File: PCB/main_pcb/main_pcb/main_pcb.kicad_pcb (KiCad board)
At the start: 2 copper layers, 163.5 x 142.5 mm, 49 parts, among them J1 Conn_01x20_Socket, J2 Conn_01x20_Socket, SW0_Header1 B6B-XH-A, SW1_Header1 B6B-XH-A

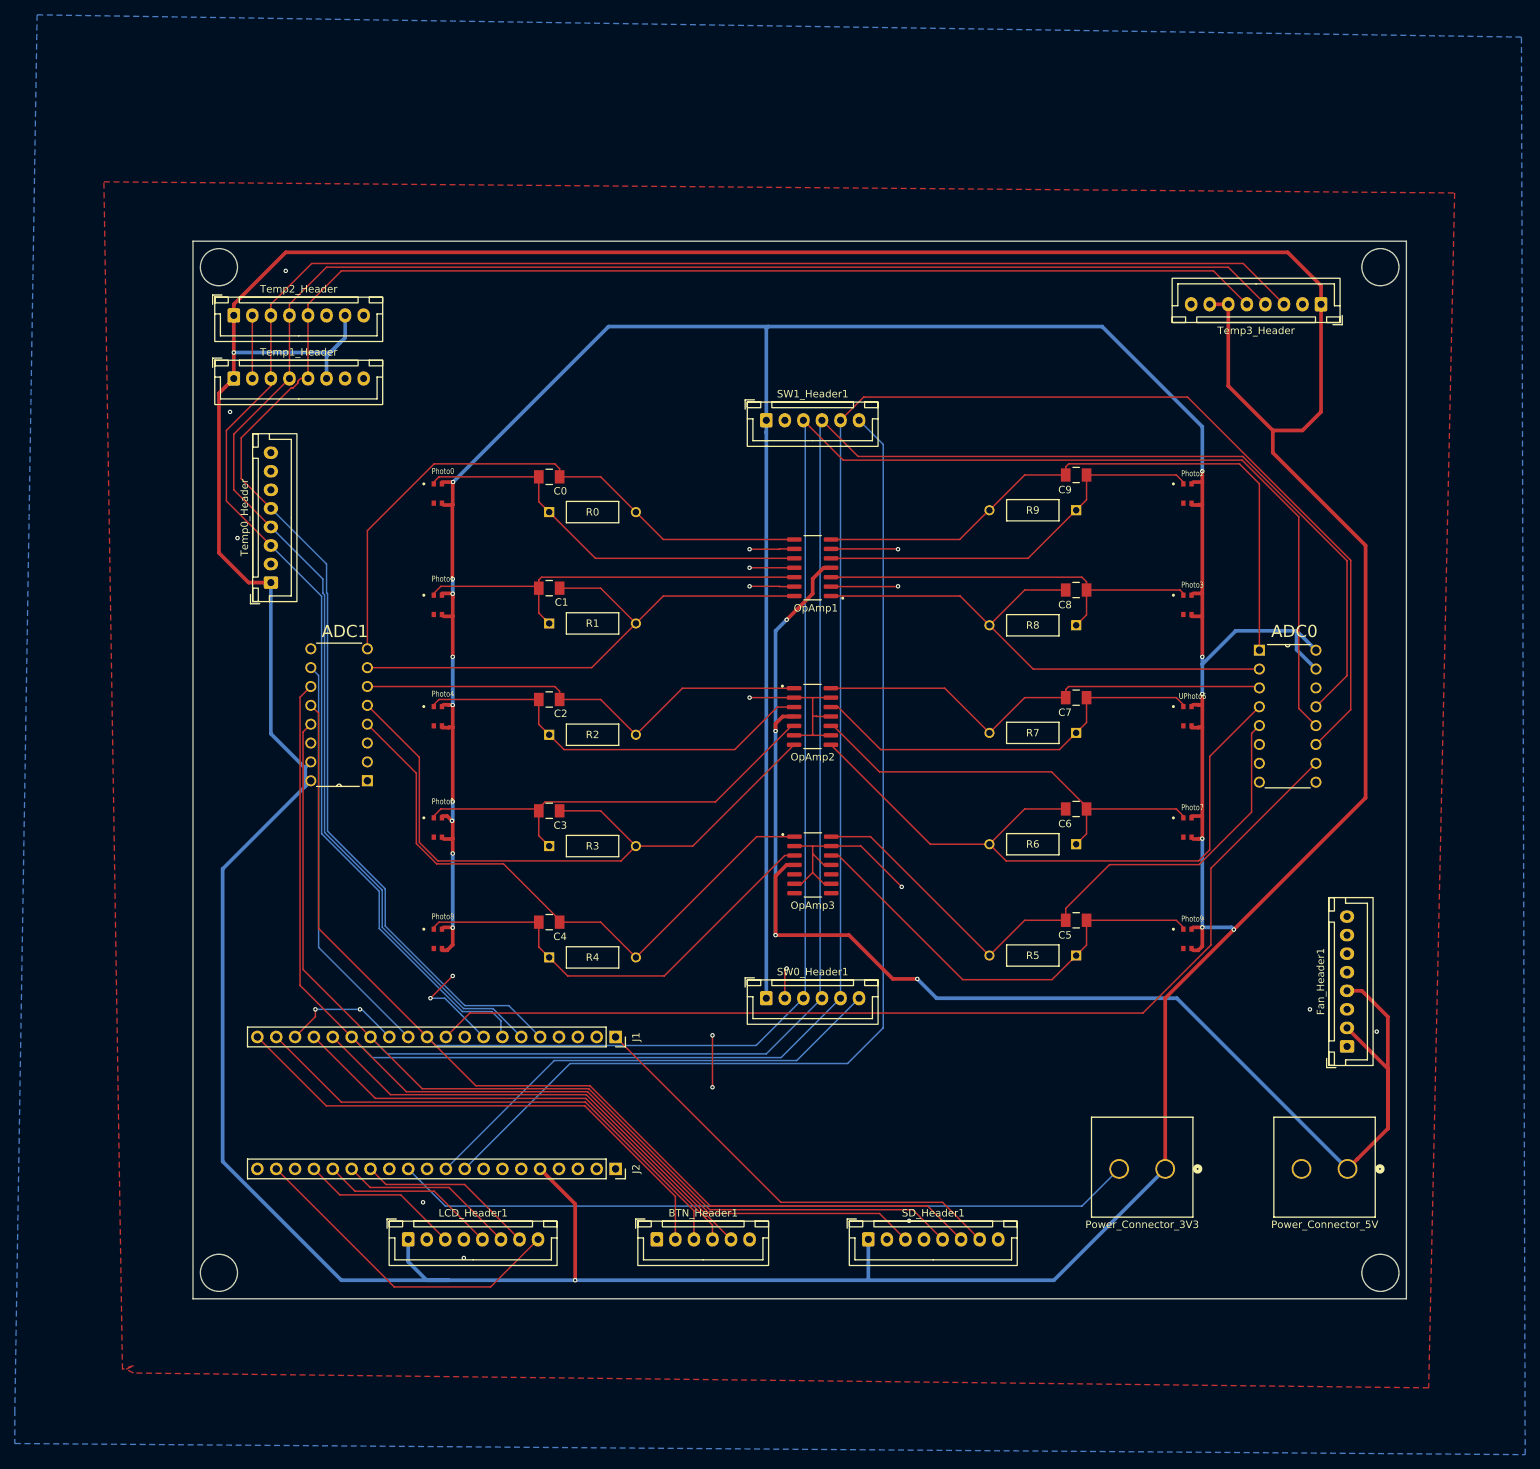
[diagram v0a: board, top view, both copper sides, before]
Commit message: Added heater actuation header.
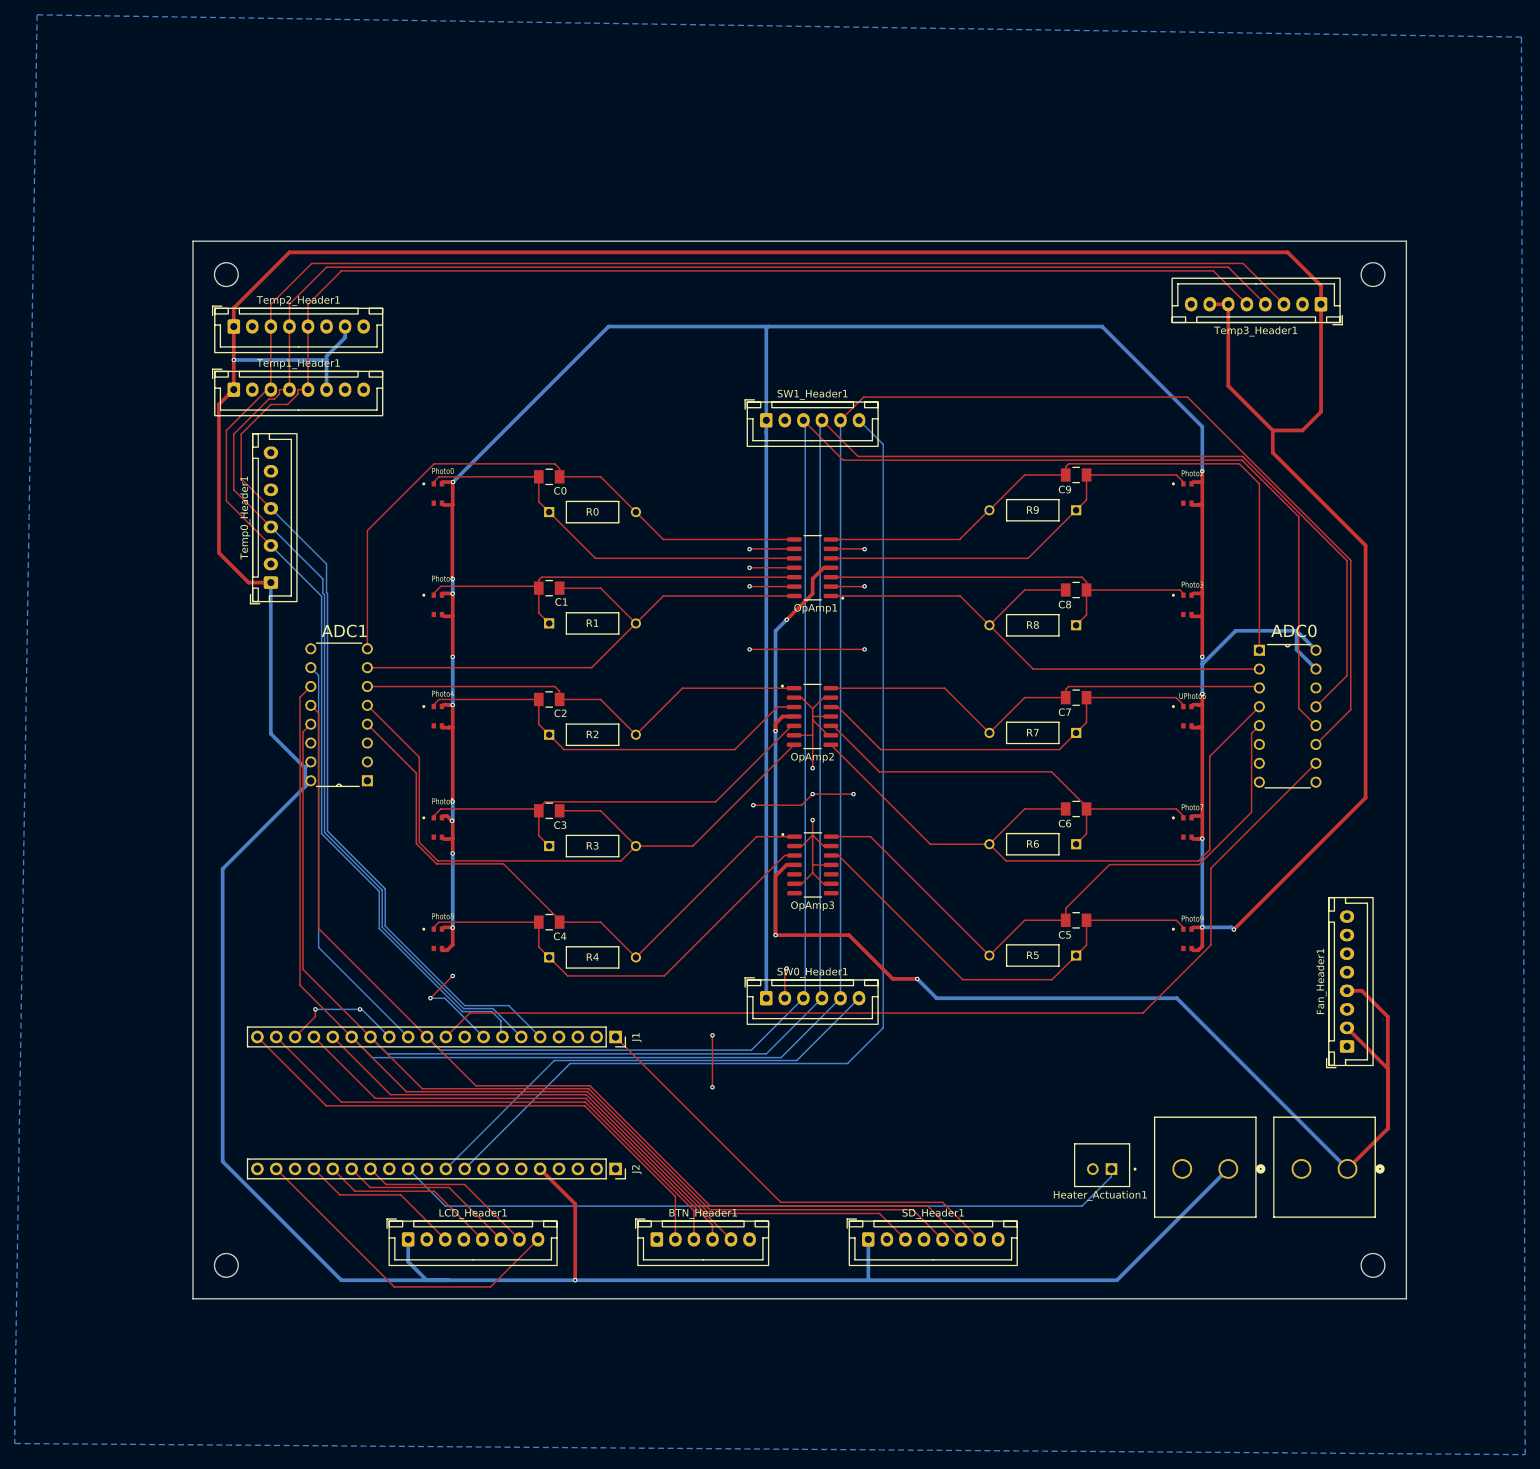
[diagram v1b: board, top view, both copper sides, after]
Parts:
- added Heater_Actuation1: B2B-XH-A, B2B_XH_A:JST_B2B-XH-A, F.Cu at (140.0, 153.0)
- added REF**: MountingHole_3.2mm_M3, MountingHole:MountingHole_3.2mm_M3, F.Cu at (176.5, 33.0)
- added REF**: MountingHole_3.2mm_M3, MountingHole:MountingHole_3.2mm_M3, F.Cu at (22.0, 33.0)
- added REF**: MountingHole_3.2mm_M3, MountingHole:MountingHole_3.2mm_M3, F.Cu at (22.0, 166.5)
- added REF**: MountingHole_3.2mm_M3, MountingHole:MountingHole_3.2mm_M3, F.Cu at (176.5, 166.5)
- moved Power_Connector_3V3 8.50 mm to (157.0, 153.5)
- moved Temp1_Header1 1.50 mm to (23.0, 48.5)
- moved Temp2_Header1 1.50 mm to (23.0, 40.0)
- renumbered Power_Connector_5V to Power_Connector_5V1, Temp0_Header to Temp0_Header1, Temp1_Header to Temp1_Header1, Temp2_Header to Temp2_Header1, Temp3_Header to Temp3_Header1
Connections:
- net SPI0_RX renamed SPI0_MISO
- net SPI0_TX renamed SPI0_MOSI
- net SPI1_RX renamed SPI1_MISO
- net SPI1_TX renamed SPI1_MOSI
- Power_Connector_3V3 pad 2: HEATER_ON -> GND
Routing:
- net +3.3V: track 1034.8 -> 1004.3 mm
- net GND: track 139.1 -> 142.5 mm, vias 22 -> 19
- net TEMP_ALERT: track 253.6 -> 254.9 mm
- net I2C0_SDA: track 255.8 -> 257.1 mm
- net SPI1_MISO: track 367.6 -> 368.1 mm
- removed copper zone on F.Cu, net GND
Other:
- outline, holes or cut-outs redrawn

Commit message: Updated and tweaked main PCB
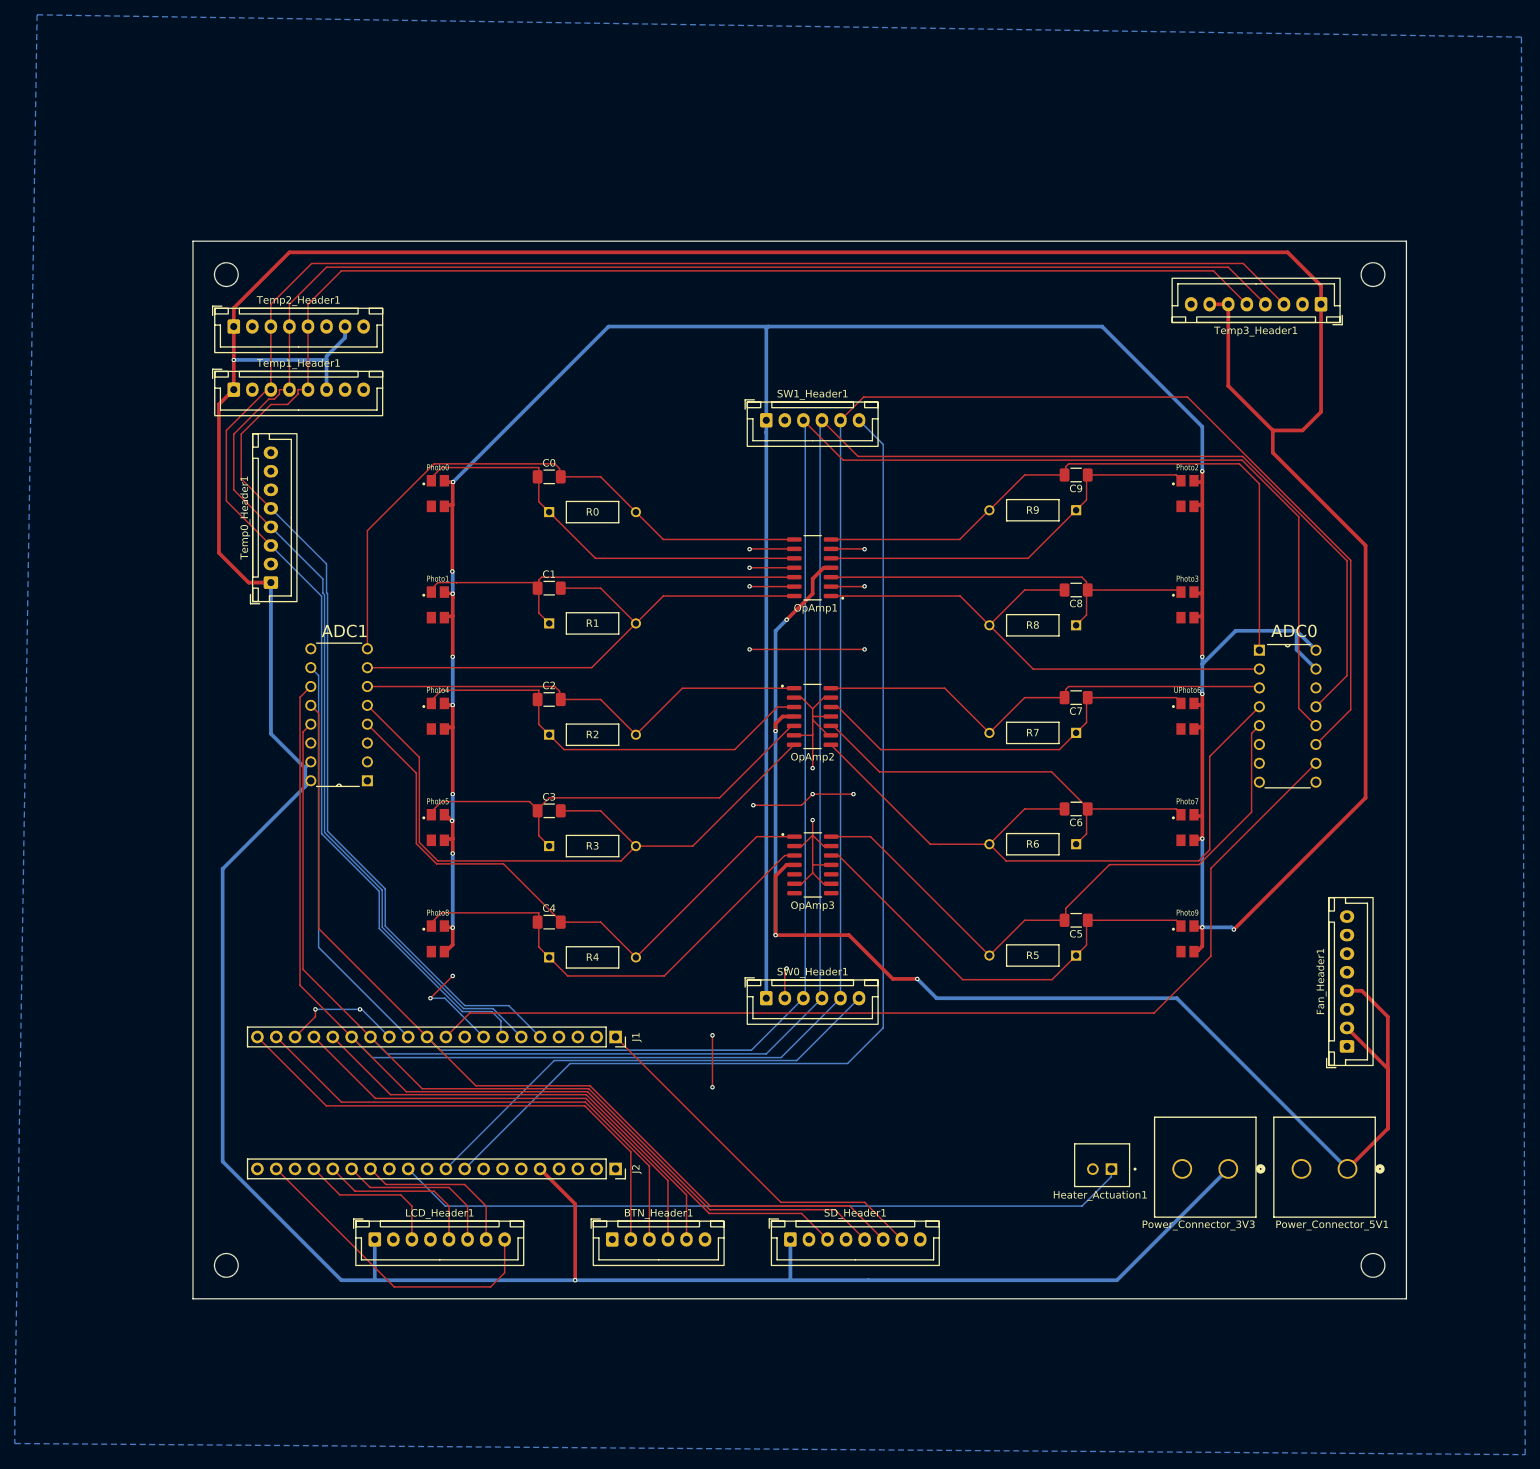
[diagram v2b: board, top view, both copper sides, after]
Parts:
- C0, C1, C2, C3, C4, C5, C6, C7, C8, C9: footprint C1206C101K1HACTU:CAPC340180_88N_KEM -> Capacitor_SMD:C_1206_3216Metric_Pad1.33x1.80mm_HandSolder
- Photo0, Photo1, Photo2, Photo3, Photo4, Photo5, Photo7, Photo8, Photo9, UPhoto6: footprint APDS_9006_020:photodiode_v3 -> APDS_9006_020:photodiode_v4
- moved SD_Header1 10.5 mm to (98.0, 163.0)
- moved BTN_Header1 6.00 mm to (74.0, 163.0)
- moved LCD_Header1 4.50 mm to (42.0, 163.0)
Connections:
- J2 pad 14: DISP REGSEL -> DISP_RST
- J2 pad 15: DISP_RST -> DISP REGSEL
- LCD_Header1 pad 6: DISP_RST -> DISP REGSEL
- LCD_Header1 pad 7: DISP REGSEL -> DISP_RST
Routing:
- net SPI1_SCK: track 377.7 -> 367.2 mm
- net SPI1_MOSI: track 390.7 -> 380.2 mm
- net SPI1_MISO: track 368.1 -> 357.6 mm
- net SPI1_CSn_SD: track 60.4 -> 49.9 mm
- net +3.3V: track 1004.3 -> 1000.3 mm
- net OpIn8: track 60.6 -> 63.3 mm
- net OpIn4: track 56.0 -> 58.5 mm
- net OpIn0: track 55.4 -> 57.9 mm
- net BTN1: track 69.8 -> 67.4 mm
- net BTN3: track 65.0 -> 62.5 mm
- net BTN2: track 66.1 -> 63.6 mm
- net BTN0: track 71.0 -> 68.5 mm
- net DISP_RST: track 24.1 -> 22.2 mm
- net SPI0_SCK: track 21.6 -> 19.8 mm
- net SPI0_MOSI: track 24.1 -> 22.2 mm
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
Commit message: Fixed some stuff and made the main PCB smaller.
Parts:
- added J3: Conn_01x09_Socket, Connector_PinSocket_2.54mm:PinSocket_1x09_P2.54mm_Vertical, F.Cu at (94.9, 146.5)
- Fan_Header1: value B8B-XH-A -> B2B-XH-A; footprint Connector_JST:JST_XH_B8B-XH-A_1x08_P2.50mm_Vertical -> B2B_XH_A:JST_B2B-XH-A
- moved Heater_Actuation1 18.7 mm to (124.5, 163.5)
- moved Power_Connector_5V1 16.2 mm to (157.5, 158.0)
- moved Power_Connector_3V3 16.1 mm to (141.5, 158.0)
- moved Temp3_Header1 15.2 mm to (176.5, 50.5)
- moved Temp0_Header1 10.0 mm to (28.0, 84.5)
- moved Temp1_Header1 10.0 mm to (23.0, 58.5)
- moved LCD_Header1 9.50 mm to (32.5, 163.0)
- moved REF** 9.00 mm to (176.5, 42.0)
- moved REF** 9.00 mm to (22.0, 42.0)
- moved Temp2_Header1 9.00 mm to (23.0, 49.0)
- moved SD_Header1 5.00 mm to (93.0, 163.0)
- moved Fan_Header1 4.03 mm to (171.5, 140.8), turned to -90 degrees
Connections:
- J1 pad 2: unconnected-(J1-Pin_2-Pad2) -> GPIO1
- J1 pad 4: unconnected-(J1-Pin_4-Pad4) -> GPIO2
- J1 pad 9: unconnected-(J1-Pin_9-Pad9) -> GPIO6
- J2 pad 11: unconnected-(J2-Pin_11-Pad11) -> RUN
- J2 pad 2: VSYS -> +3.3V
- J2 pad 20: SPI0_MISO -> GPIO16
- J2 pad 5: +3.3V -> 3V3_OUT
- J2 pad 7: unconnected-(J2-Pin_7-Pad7) -> GPIO29
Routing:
- net GPIO16: track 0.00 -> 94.0 mm, vias 0 -> 2
- net RUN: track 0.00 -> 69.4 mm
- net GPIO29: track 0.00 -> 56.3 mm
- net ADC_VREF: track 0.00 -> 50.8 mm
- net 3V3_OUT: track 0.00 -> 45.4 mm
- net 3V3_EN: track 0.00 -> 39.6 mm
- net GPIO2: track 0.00 -> 37.9 mm
- net +5V: track 203.9 -> 169.2 mm
- net VBUS: track 0.00 -> 28.5 mm
- net GPIO1: track 0.00 -> 28.4 mm
- net HEATER_ON: track 99.5 -> 83.6 mm
- net SPI0_CSn: track 42.7 -> 31.7 mm
- net SPI0_MOSI: track 22.2 -> 12.1 mm
- net DISP REGSEL: track 22.2 -> 12.0 mm
- net DISP_RST: track 22.2 -> 12.0 mm
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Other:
- board size 163.5 x 142.5 mm -> 163.5 x 133.5 mm
- board text added: "3V3_EN"
- board text added: "3V3_OUT"
- board text added: "ADC_REF"
- board text added: "GP1"
- board text added: "GP16"
- board text added: "GP2"
- board text added: "GP29"
- board text added: "RUN"
- board text added: "VBUS"
